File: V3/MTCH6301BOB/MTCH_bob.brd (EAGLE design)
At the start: 34.3 x 27.3 mm, 38 parts, among them J2 LiPo, U2 MTCH6301-I/ML, U4 AP2112K-3.3TRG-1

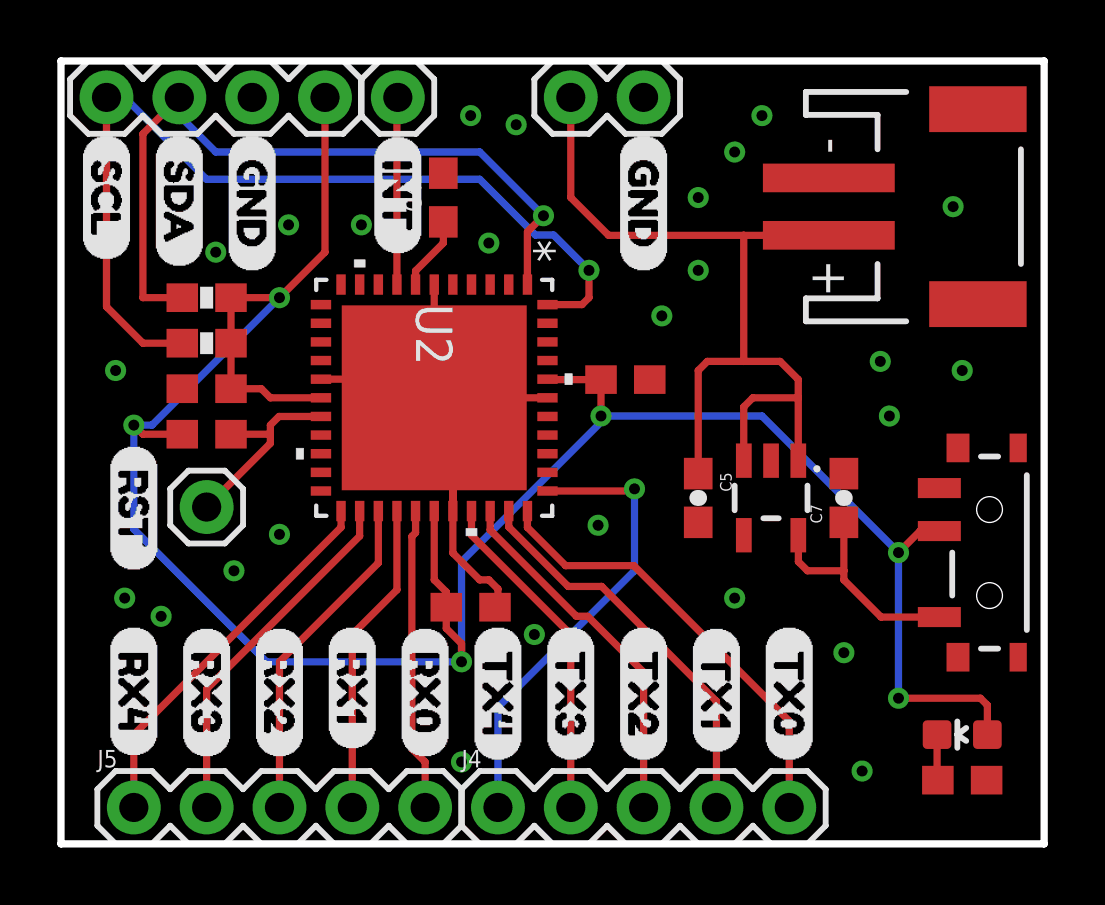
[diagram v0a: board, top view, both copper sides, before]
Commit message: updated MTCH6301 breakout board because of out of stock parts
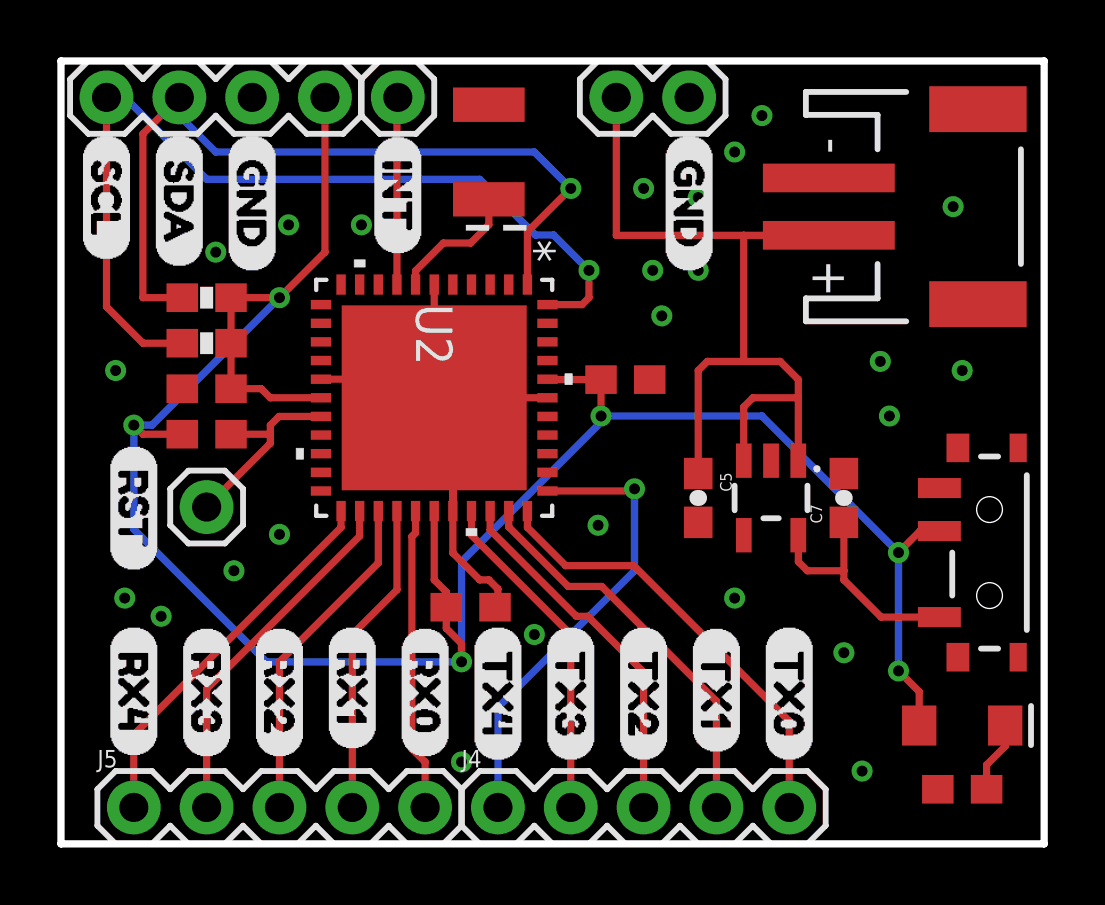
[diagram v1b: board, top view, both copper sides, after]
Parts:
- C4: device SparkFun-Capacitors:0603 -> SparkFun-Capacitors:EIA3528
- D4: value POWER -> RED; device SparkFun-LED:LED-0603 -> SparkFun-LED:LED-1206
- moved C4 2.25 mm to (14.9, 24.1), turned to 270 degrees
- moved J6 1.59 mm to (21.9, 26.0)
- moved U$16 1.59 mm to (21.9, 24.8)
- moved D4 0.32 mm to (31.4, 4.13), turned to 0 degrees
- moved R2 0.32 mm to (31.4, 1.91), turned to 0 degrees
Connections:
- net GND: now also C4.C; no longer C4.2
- net N$2: now also C4.A; no longer C4.1
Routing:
- net VCC: track 84.3 -> 81.3 mm
- net N$2: track 2.59 -> 4.65 mm
- net SDA: track 26.3 -> 28.2 mm
- net N$4: track 1.60 -> 2.49 mm
- net LIPO: track 31.7 -> 30.8 mm
- net GND: vias 26 -> 25
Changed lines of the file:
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@@
 <attribute name="PROD_ID" value="CAP-00810" x="-31.75" y="46.355" size="1.778" layer="27" rot="R180" display="off"/>
-</element>
-<element name="C4" library="SparkFun-Capacitors" library_urn="urn:adsk.eagle:library:510" package="0603" package3d_urn="urn:adsk.eagle:package:37414/1" value="10uF" x="13.335" y="22.5425" smashed="yes" rot="R90">
-<attribute name="NAME" x="12.573" y="22.5425" size="0.6096" layer="25" font="vector" ratio="20" rot="R90" align="bottom-center"/>
-<attribute name="PROD_ID" value="CAP-11015" x="47.625" y="37.7825" size="1.778" layer="27" rot="R90" display="off"/>
 </element>
 <element name="C5" library="SparkFun-Passives" package="0603-CAP" value="1uF" x="22.225" y="12.065" smashed="yes" rot="R270">
@@
 <attribute name="VALUE" x="1.27" y="-0.762" size="0.6096" layer="27" font="vector" ratio="20"/>
 </element>
-<element name="J6" library="SparkFun-Connectors" library_urn="urn:adsk.eagle:library:513" package="1X02" package3d_urn="urn:adsk.eagle:package:38039/1" value="" x="20.32" y="26.035" smashed="yes" rot="R180">
-<attribute name="VALUE" x="21.59" y="28.067" size="0.6096" layer="27" font="vector" ratio="20" rot="R180"/>
+<element name="J6" library="SparkFun-Connectors" library_urn="urn:adsk.eagle:library:513" package="1X02" package3d_urn="urn:adsk.eagle:package:38039/1" value="" x="21.9075" y="26.035" smashed="yes" rot="R180">
+<attribute name="VALUE" x="23.1775" y="28.067" size="0.6096" layer="27" font="vector" ratio="20" rot="R180"/>
 </element>
 <element name="J7" library="SparkFun-Connectors" library_urn="urn:adsk.eagle:library:513" package="1X01" package3d_urn="urn:adsk.eagle:package:38028/1" value="" x="5.08" y="11.7475" smashed="yes">
@@
 <element name="U$14" library="buzzard_labels (27)" package="TX35" value="" x="17.78" y="7.62" smashed="yes" rot="R270"/>
 <element name="U$15" library="buzzard_labels (27)" package="TX46" value="" x="15.24" y="7.62" smashed="yes" rot="R270"/>
-<element name="U$16" library="buzzard_labels (27)" package="GND0" value="" x="20.32" y="24.765" smashed="yes" rot="R270"/>
+<element name="U$16" library="buzzard_labels (27)" package="GND0" value="" x="21.9075" y="24.765" smashed="yes" rot="R270"/>
 <element name="U$17" library="buzzard_labels (27)" package="TX24" value="" x="20.32" y="7.62" smashed="yes" rot="R270"/>
-<element name="D4" library="SparkFun-LED" package="LED-0603" value="POWER" x="31.4325" y="3.81" smashed="yes" rot="R90">
-<attribute name="PROD_ID" value="DIO-00821" x="20.0025" y="-1.27" size="1.778" layer="27" font="vector" ratio="15" rot="R90" display="off"/>
-</element>
-<element name="R2" library="SparkFun-Resistors" package="0603" value="1k" x="31.4325" y="2.2225" smashed="yes" rot="R180">
-<attribute name="PROD_ID" value="RES-07856" x="31.4325" y="2.2225" size="1.778" layer="27" font="vector" ratio="15" rot="R180" display="off"/>
+<element name="D4" library="SparkFun-LED" library_urn="urn:adsk.eagle:library:529" package="LED-1206" package3d_urn="urn:adsk.eagle:package:39352/1" value="RED" x="31.4325" y="4.1275" smashed="yes">
+<attribute name="PROD_ID" value="DIO-09912" x="26.3525" y="15.5575" size="1.778" layer="27" font="vector" ratio="15" display="off"/>
+</element>
+<element name="R2" library="SparkFun-Resistors" package="0603" value="1k" x="31.4325" y="1.905" smashed="yes">
+<attribute name="PROD_ID" value="RES-07856" x="31.4325" y="1.905" size="1.778" layer="27" font="vector" ratio="15" display="off"/>
+</element>
+<element name="C4" library="SparkFun-Capacitors" library_urn="urn:adsk.eagle:library:510" package="EIA3528" package3d_urn="urn:adsk.eagle:package:37411/1" value="10uF" x="14.9225" y="24.13" smashed="yes" rot="R270">
+<attribute name="PROD_ID" value="CAP-08063" x="14.9225" y="24.13" size="1.778" layer="27" rot="R270" display="off"/>
 </element>
 </elements>
@@
 <contactref element="J2" pad="1"/>
 <contactref element="J1" pad="3"/>
-<contactref element="C4" pad="2"/>
 <contactref element="U2" pad="6"/>
 <contactref element="U2" pad="39"/>
@@
 <via x="23.495" y="24.13" extent="1-16" drill="0.381"/>
 <via x="22.225" y="22.5425" extent="1-16" drill="0.381"/>
-<via x="15.875" y="25.0825" extent="1-16" drill="0.381"/>
+<via x="20.6375" y="20.0025" extent="1-16" drill="0.381"/>
 <via x="10.4775" y="21.59" extent="1-16" drill="0.381"/>
 <via x="7.9375" y="21.59" extent="1-16" drill="0.381"/>
@@
 <wire x1="15.24" y1="8.3575" x2="15.1375" y2="8.255" width="0.254" layer="1"/>
 <wire x1="13.6675" y1="10.145" x2="14.605" y2="9.2075" width="0.254" layer="1"/>
-<via x="14.2875" y="25.4" extent="1-16" drill="0.381"/>
-<via x="14.9225" y="20.955" extent="1-16" drill="0.381"/>
+<via x="20.32" y="22.86" extent="1-16" drill="0.381"/>
 <via x="22.225" y="20.0025" extent="1-16" drill="0.381"/>
 <via x="24.4475" y="25.4" extent="1-16" drill="0.381"/>
@@
 <via x="3.4925" y="7.9375" extent="1-16" drill="0.381"/>
 <via x="6.0325" y="9.525" extent="1-16" drill="0.381"/>
+<contactref element="C4" pad="C"/>
 </signal>
 <signal name="VCC">
@@
 <wire x1="2.8575" y1="14.2875" x2="2.54" y2="14.605" width="0.254" layer="1"/>
 <via x="2.54" y="14.605" extent="1-16" drill="0.381"/>
-<wire x1="32.3095" y1="3.81" x2="32.3095" y2="4.838" width="0.254" layer="1"/>
-<wire x1="32.3095" y1="4.838" x2="32.0675" y2="5.08" width="0.254" layer="1"/>
-<wire x1="32.0675" y1="5.08" x2="29.21" y2="5.08" width="0.254" layer="1"/>
-<via x="29.21" y="5.08" extent="1-16" drill="0.381"/>
-<wire x1="29.21" y1="10.16" x2="29.21" y2="5.08" width="0.254" layer="16"/>
+<via x="29.21" y="6.0325" extent="1-16" drill="0.381"/>
+<wire x1="29.21" y1="10.16" x2="29.21" y2="6.0325" width="0.254" layer="16"/>
 <via x="29.21" y="10.16" extent="1-16" drill="0.381"/>
 <wire x1="2.54" y1="10.9757875" x2="2.54" y2="14.605" width="0.254" layer="16"/>
@@
 <wire x1="29.21" y1="10.16" x2="24.4475" y2="14.9225" width="0.254" layer="16"/>
 <wire x1="24.4475" y1="14.9225" x2="18.835" y2="14.9225" width="0.254" layer="16"/>
+<wire x1="29.21" y1="6.0325" x2="29.9325" y2="5.31" width="0.254" layer="1"/>
+<wire x1="29.9325" y1="5.31" x2="29.9325" y2="4.1275" width="0.254" layer="1"/>
 </signal>
 <signal name="LIPO">
@@
 <contactref element="J6" pad="2"/>
 <wire x1="26.78" y1="21.225" x2="23.8125" y2="21.225" width="0.254" layer="1"/>
-<wire x1="23.8125" y1="21.225" x2="19.0975" y2="21.225" width="0.254" layer="1"/>
-<wire x1="19.0975" y1="21.225" x2="17.78" y2="22.5425" width="0.254" layer="1"/>
-<wire x1="17.78" y1="22.5425" x2="17.78" y2="26.035" width="0.254" layer="1"/>
+<wire x1="23.8125" y1="21.225" x2="19.3675" y2="21.225" width="0.254" layer="1"/>
+<wire x1="19.3675" y1="21.225" x2="19.3675" y2="26.035" width="0.254" layer="1"/>
 <wire x1="25.715" y1="13.3651" x2="25.715" y2="15.5575" width="0.254" layer="1"/>
 <wire x1="25.715" y1="15.5575" x2="25.715" y2="16.195" width="0.254" layer="1"/>
@@
 <wire x1="2.8575" y1="24.765" x2="4.1275" y2="26.035" width="0.254" layer="1"/>
 <wire x1="16.2675" y1="19.5072" x2="16.2675" y2="21.3475" width="0.254" layer="1"/>
-<wire x1="16.2675" y1="21.3475" x2="16.8275" y2="21.9075" width="0.254" layer="1"/>
-<via x="16.8275" y="21.9075" extent="1-16" drill="0.381"/>
-<wire x1="16.8275" y1="21.9075" x2="14.605" y2="24.13" width="0.254" layer="16"/>
-<wire x1="14.605" y1="24.13" x2="5.3975" y2="24.13" width="0.254" layer="16"/>
+<wire x1="16.2675" y1="21.3475" x2="17.78" y2="22.86" width="0.254" layer="1"/>
+<via x="17.78" y="22.86" extent="1-16" drill="0.381"/>
+<wire x1="17.78" y1="22.86" x2="16.51" y2="24.13" width="0.254" layer="16"/>
+<wire x1="16.51" y1="24.13" x2="5.3975" y2="24.13" width="0.254" layer="16"/>
 <wire x1="5.3975" y1="24.13" x2="4.1275" y2="25.4" width="0.254" layer="16"/>
 <wire x1="4.1275" y1="25.4" x2="4.1275" y2="26.035" width="0.254" layer="16"/>
@@
 <signal name="N$2">
 <contactref element="U2" pad="7"/>
-<contactref element="C4" pad="1"/>
 <wire x1="12.3675" y1="19.9875" x2="12.3675" y2="19.5072" width="0.254" layer="1"/>
-<wire x1="13.335" y1="21.6925" x2="13.335" y2="20.955" width="0.254" layer="1"/>
 <wire x1="13.335" y1="20.955" x2="12.3675" y2="19.9875" width="0.254" layer="1"/>
+<contactref element="C4" pad="A"/>
+<wire x1="14.86" y1="22.48" x2="14.9225" y2="22.48" width="0.1778" layer="1"/>
+<wire x1="14.9225" y1="22.48" x2="14.9225" y2="21.59" width="0.254" layer="1"/>
+<wire x1="14.2875" y1="20.955" x2="13.335" y2="20.955" width="0.254" layer="1"/>
+<wire x1="14.9225" y1="21.59" x2="14.2875" y2="20.955" width="0.254" layer="1"/>
 </signal>
 <signal name="RST">
@@
 <contactref element="D4" pad="C"/>
 <contactref element="R2" pad="2"/>
-<wire x1="30.5825" y1="2.2225" x2="30.5555" y2="2.2495" width="0.254" layer="1"/>
-<wire x1="30.5555" y1="2.2495" x2="30.5555" y2="3.81" width="0.254" layer="1"/>
+<wire x1="32.9325" y1="4.1275" x2="32.9325" y2="3.405" width="0.254" layer="1"/>
+<wire x1="32.2825" y1="2.755" x2="32.2825" y2="1.905" width="0.254" layer="1"/>
+<wire x1="32.9325" y1="3.405" x2="32.2825" y2="2.755" width="0.254" layer="1"/>
 </signal>
 </signals>
